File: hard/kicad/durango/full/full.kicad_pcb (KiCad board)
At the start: 2 copper layers, 98 parts, among them J1 NANOLINK, J105 SCART, J2 AUDIO IN, J206 VIDEO, J3 IOX9, J4 BUZZER, J7 POWER, J8 DEBUG, Q1 BC547, Q106 BC547, Q2 BC547, Q3 BC547, Q4 BC547, Q5 BC547, SW1 RESET, SW2 NMI, U1 65C02, U10 74HC139, U104 74HC257, U105 74HC257, U11 74HC688, U12 74HC74, U124 74HC574, U125 74HC257, U126 HC86, U127 74HC245, U13 74HC32, U14 74HC4040, U15 74HCT4040, U16 74HC02, U17 74HC21, U18 74HC85, U19 74HC4040, U2 27C256, U20 74HC85, U204 74HC257, U205 74HC257, U22 74HC175, U224 74HC166, U227 74HC20, U23 74HC86, U3 62256, U31 74HC245, U32 74HC365, U321 74HC257, U528 74HC174, U529 74HC139, U530 74HC367, U6 74HC257, U7 74HC257, U8 74HC132, U9 74HC00, X1 24.576 MHz

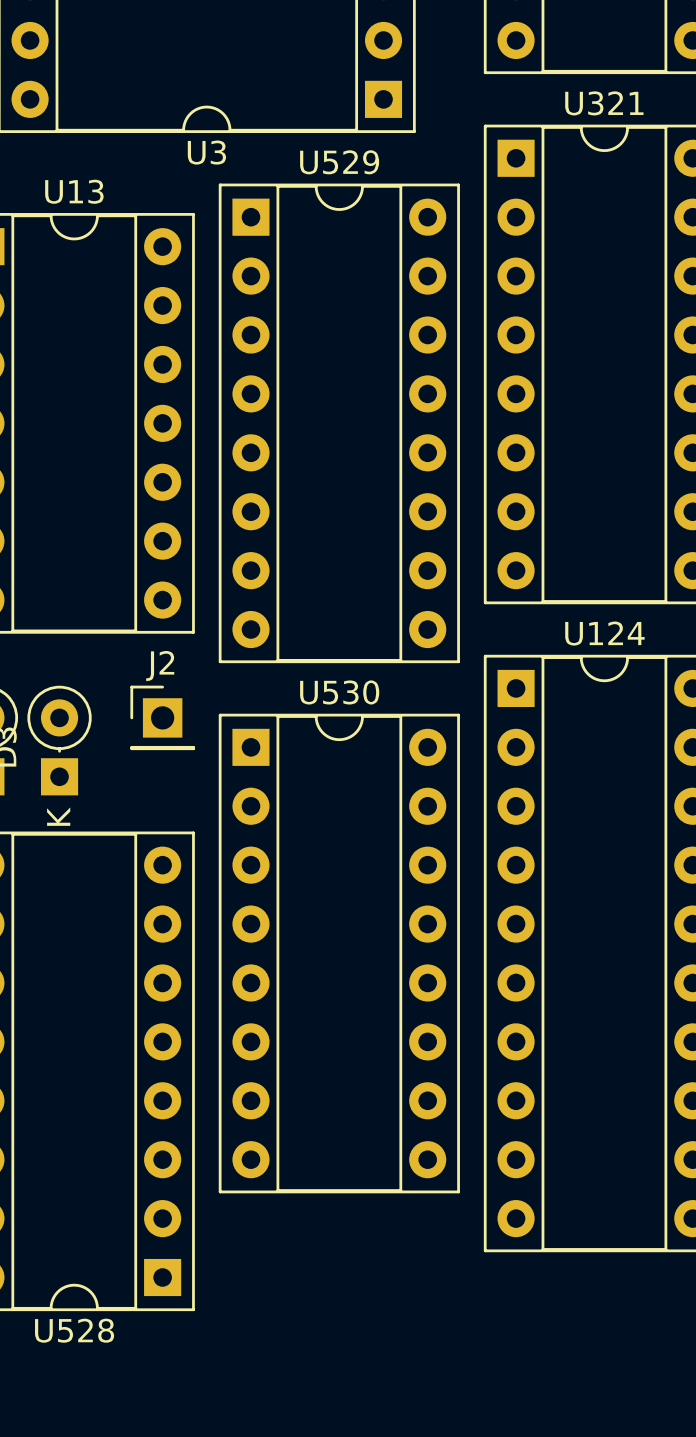
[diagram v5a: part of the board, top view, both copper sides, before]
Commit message: faster extra IO
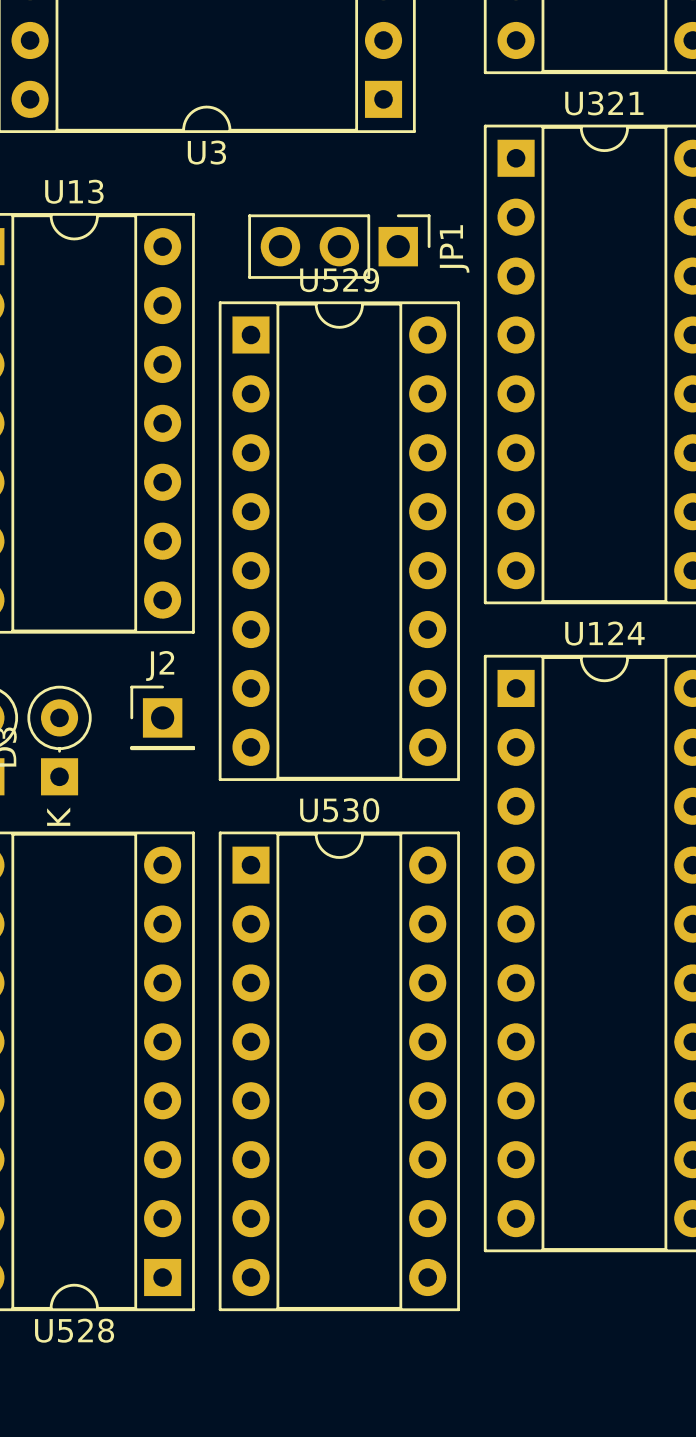
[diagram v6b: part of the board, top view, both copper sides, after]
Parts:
- added JP1: FAST/TIGHT, Connector_PinHeader_2.54mm:PinHeader_1x03_P2.54mm_Vertical, F.Cu at (163.8, 97.8)
- moved U529 5.08 mm to (157.5, 101.6)
- moved U530 5.08 mm to (157.5, 124.5)
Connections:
- U10 pad 13: SCLK -> VCLK
- U529 pad 1: /VDU-X/~IA08 -> /VDU-X/~VFEN
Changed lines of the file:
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@@
     (tracks 215)
     (zones 0)
-    (modules 98)
-    (nets 183)
+    (modules 99)
+    (nets 184)
   )
   (page A4)
@@
   (net 181 /VDU-X/DHRDE)
   (net 182 /VDU-X/HVID)
+  (net 183 /VDU-X/~VFEN)
   (net_class Default "Esta es la clase de red por defecto."
     (clearance 0.2)
@@
     (add_net /VDU-X/~PE)
     (add_net /VDU-X/~VA0)
+    (add_net /VDU-X/~VFEN)
     (add_net /~DWE)
     (add_net /~HIRES)
@@
     (add_net "Net-(D4-Pad2)")
     (add_net "Net-(D6-Pad2)")
+    (add_net "Net-(J105-Pad1)")
+    (add_net "Net-(J105-Pad10)")
+    (add_net "Net-(J105-Pad12)")
+    (add_net "Net-(J105-Pad14)")
+    (add_net "Net-(J105-Pad17)")
+    (add_net "Net-(J105-Pad19)")
+    (add_net "Net-(J105-Pad3)")
     (add_net "Net-(J4-Pad2)")
+    (add_net "Net-(J7-Pad2)")
+    (add_net "Net-(J7-Pad3)")
+    (add_net "Net-(J8-Pad3)")
     (add_net "Net-(Q1-Pad2)")
     (add_net "Net-(Q106-Pad3)")
     (add_net "Net-(Q2-Pad2)")
     (add_net "Net-(Q4-Pad3)")
+    (add_net "Net-(U1-Pad3)")
+    (add_net "Net-(U1-Pad35)")
+    (add_net "Net-(U1-Pad36)")
+    (add_net "Net-(U1-Pad5)")
+    (add_net "Net-(U1-Pad7)")
+    (add_net "Net-(U10-Pad10)")
+    (add_net "Net-(U10-Pad11)")
+    (add_net "Net-(U10-Pad12)")
+    (add_net "Net-(U12-Pad6)")
     (add_net "Net-(U124-Pad12)")
     (add_net "Net-(U124-Pad13)")
@@
     (add_net "Net-(U126-Pad8)")
     (add_net "Net-(U14-Pad1)")
+    (add_net "Net-(U14-Pad12)")
+    (add_net "Net-(U14-Pad13)")
+    (add_net "Net-(U14-Pad14)")
     (add_net "Net-(U14-Pad15)")
+    (add_net "Net-(U14-Pad2)")
+    (add_net "Net-(U14-Pad3)")
+    (add_net "Net-(U14-Pad4)")
+    (add_net "Net-(U14-Pad5)")
+    (add_net "Net-(U14-Pad6)")
+    (add_net "Net-(U14-Pad7)")
+    (add_net "Net-(U14-Pad9)")
+    (add_net "Net-(U15-Pad1)")
     (add_net "Net-(U15-Pad10)")
+    (add_net "Net-(U15-Pad9)")
+    (add_net "Net-(U18-Pad5)")
+    (add_net "Net-(U18-Pad7)")
+    (add_net "Net-(U19-Pad1)")
+    (add_net "Net-(U19-Pad14)")
+    (add_net "Net-(U19-Pad15)")
+    (add_net "Net-(U20-Pad5)")
+    (add_net "Net-(U20-Pad7)")
+    (add_net "Net-(U22-Pad10)")
     (add_net "Net-(U22-Pad11)")
     (add_net "Net-(U22-Pad14)")
+    (add_net "Net-(U22-Pad15)")
+    (add_net "Net-(U22-Pad3)")
+    (add_net "Net-(U22-Pad7)")
     (add_net "Net-(U23-Pad3)")
+    (add_net "Net-(U32-Pad13)")
+    (add_net "Net-(U528-Pad2)")
+    (add_net "Net-(U529-Pad10)")
+    (add_net "Net-(U529-Pad11)")
+    (add_net "Net-(U529-Pad6)")
+    (add_net "Net-(U529-Pad9)")
     (add_net "Net-(U8-Pad3)")
+    (add_net "Net-(X1-Pad1)")
     (add_net R~W)
     (add_net SC0)
@@
     (add_net ~STAT)
   )
+  (module Connector_PinHeader_2.54mm:PinHeader_1x03_P2.54mm_Vertical (layer F.Cu)
+    (at 163.83 97.79 270)
+    (descr "Through hole straight pin header, 1x03, 2.54mm pitch, single row")
+    (tags "Through hole pin header THT 1x03 2.54mm single row")
+    (fp_text reference JP1 (at 0 -2.33 90) (layer F.SilkS)
+      (effects (font (size 1 1) (thickness 0.15)))
+    )
+    (fp_text value FAST/TIGHT (at 0 7.41 90) (layer F.Fab)
+      (effects (font (size 1 1) (thickness 0.15)))
+    )
+    (fp_text user %R (at 0 2.54) (layer F.Fab)
+      (effects (font (size 1 1) (thickness 0.15)))
+    )
+    (fp_line (start 1.8 -1.8) (end -1.8 -1.8) (layer F.CrtYd) (width 0.05))
+    (fp_line (start 1.8 6.85) (end 1.8 -1.8) (layer F.CrtYd) (width 0.05))
+    (fp_line (start -1.8 6.85) (end 1.8 6.85) (layer F.CrtYd) (width 0.05))
+    (fp_line (start -1.8 -1.8) (end -1.8 6.85) (layer F.CrtYd) (width 0.05))
+    (fp_line (start -1.33 -1.33) (end 0 -1.33) (layer F.SilkS) (width 0.12))
+    (fp_line (start -1.33 0) (end -1.33 -1.33) (layer F.SilkS) (width 0.12))
+    (fp_line (start -1.33 1.27) (end 1.33 1.27) (layer F.SilkS) (width 0.12))
+    (fp_line (start 1.33 1.27) (end 1.33 6.41) (layer F.SilkS) (width 0.12))
+    (fp_line (start -1.33 1.27) (end -1.33 6.41) (layer F.SilkS) (width 0.12))
+    (fp_line (start -1.33 6.41) (end 1.33 6.41) (layer F.SilkS) (width 0.12))
+    (fp_line (start -1.27 -0.635) (end -0.635 -1.27) (layer F.Fab) (width 0.1))
+    (fp_line (start -1.27 6.35) (end -1.27 -0.635) (layer F.Fab) (width 0.1))
+    (fp_line (start 1.27 6.35) (end -1.27 6.35) (layer F.Fab) (width 0.1))
+    (fp_line (start 1.27 -1.27) (end 1.27 6.35) (layer F.Fab) (width 0.1))
+    (fp_line (start -0.635 -1.27) (end 1.27 -1.27) (layer F.Fab) (width 0.1))
+    (pad 3 thru_hole oval (at 0 5.08 270) (size 1.7 1.7) (drill 1) (layers *.Cu *.Mask)
+      (net 166 /VDU-X/~IA08))
+    (pad 2 thru_hole oval (at 0 2.54 270) (size 1.7 1.7) (drill 1) (layers *.Cu *.Mask)
+      (net 183 /VDU-X/~VFEN))
+    (pad 1 thru_hole rect (at 0 0 270) (size 1.7 1.7) (drill 1) (layers *.Cu *.Mask)
+      (net 34 ~IO8Q))
+    (model ${KISYS3DMOD}/Connector_PinHeader_2.54mm.3dshapes/PinHeader_1x03_P2.54mm_Vertical.wrl
+      (at (xyz 0 0 0))
+      (scale (xyz 1 1 1))
+      (rotate (xyz 0 0 0))
+    )
+  )
   (module Resistor_THT:R_Axial_DIN0204_L3.6mm_D1.6mm_P2.54mm_Vertical (layer F.Cu)
     (at 191.77 92.075)
@@
   )
   (module Package_DIP:DIP-16_W7.62mm_Socket (layer F.Cu)
-    (at 157.48 119.38)
+    (at 157.48 124.46)
     (descr "16-lead though-hole mounted DIP package, row spacing 7.62 mm (300 mils), Socket")
     (tags "THT DIP DIL PDIP 2.54mm 7.62mm 300mil Socket")
@@
   )
   (module Package_DIP:DIP-16_W7.62mm_Socket (layer F.Cu)
-    (at 157.48 96.52)
+    (at 157.48 101.6)
     (descr "16-lead though-hole mounted DIP package, row spacing 7.62 mm (300 mils), Socket")
     (tags "THT DIP DIL PDIP 2.54mm 7.62mm 300mil Socket")
@@
     (pad 9 thru_hole oval (at 7.62 17.78) (size 1.6 1.6) (drill 0.8) (layers *.Cu *.Mask))
     (pad 1 thru_hole rect (at 0 0) (size 1.6 1.6) (drill 0.8) (layers *.Cu *.Mask)
-      (net 166 /VDU-X/~IA08))
+      (net 183 /VDU-X/~VFEN))
     (model ${KISYS3DMOD}/Package_DIP.3dshapes/DIP-16_W7.62mm_Socket.wrl
       (at (xyz 0 0 0))
@@
       (net 52 /~IOAQ))
     (pad 13 thru_hole oval (at 7.62 7.62) (size 1.6 1.6) (drill 0.8) (layers *.Cu *.Mask)
-      (net 41 SCLK))
+      (net 120 VCLK))
     (pad 5 thru_hole oval (at 0 10.16) (size 1.6 1.6) (drill 0.8) (layers *.Cu *.Mask)
       (net 40 /~IO9Q))

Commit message: PCB updates
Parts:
- added J4: BUZZER, Connector_PinHeader_2.54mm:PinHeader_1x04_P2.54mm_Vertical, F.Cu at (223.5, 78.7)
- added R23: 22, Resistor_THT:R_Axial_DIN0204_L3.6mm_D1.6mm_P2.54mm_Vertical, F.Cu at (224.8, 94.0)
- C1: value 1uF -> 10uF
- C2: value 470nF -> 100nF
- C3: value 47uF -> 10uF
- C4: value 10uF -> 100uF
- C5: value 470uF -> 100uF
- D4: value INT. DISABLED -> ERROR
- R3: value 22K -> 3K3
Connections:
- C4 pad 1: /VDU-X/BIAS -> +5V
- J105 pad 1: (no net) -> Net-(J105-Pad1)
- J105 pad 10: (no net) -> Net-(J105-Pad10)
- J105 pad 12: (no net) -> Net-(J105-Pad12)
- J105 pad 14: (no net) -> Net-(J105-Pad14)
- J105 pad 17: (no net) -> Net-(J105-Pad17)
- J105 pad 19: (no net) -> Net-(J105-Pad19)
- J105 pad 3: (no net) -> Net-(J105-Pad3)
- J7 pad 2: (no net) -> Net-(J7-Pad2)
- J7 pad 3: (no net) -> Net-(J7-Pad3)
- J8 pad 3: (no net) -> Net-(J8-Pad3)
- Q3 pad 3: Net-(J4-Pad2) -> Net-(Q3-Pad3)
- R4 pad 2: Net-(J4-Pad2) -> Net-(Q3-Pad3)
- U1 pad 3: (no net) -> Net-(U1-Pad3)
- U1 pad 35: (no net) -> Net-(U1-Pad35)
- U1 pad 36: (no net) -> Net-(U1-Pad36)
- U1 pad 5: (no net) -> Net-(U1-Pad5)
- U1 pad 7: (no net) -> Net-(U1-Pad7)
- U10 pad 10: (no net) -> Net-(U10-Pad10)
- U10 pad 11: (no net) -> Net-(U10-Pad11)
- U10 pad 12: (no net) -> Net-(U10-Pad12)
- U12 pad 6: (no net) -> Net-(U12-Pad6)
- U14 pad 12: (no net) -> Net-(U14-Pad12)
- U14 pad 13: (no net) -> Net-(U14-Pad13)
- U14 pad 14: (no net) -> Net-(U14-Pad14)
- U14 pad 2: (no net) -> Net-(U14-Pad2)
- U14 pad 3: (no net) -> Net-(U14-Pad3)
- U14 pad 4: (no net) -> Net-(U14-Pad4)
- U14 pad 5: (no net) -> Net-(U14-Pad5)
- U14 pad 6: (no net) -> Net-(U14-Pad6)
- U14 pad 7: (no net) -> Net-(U14-Pad7)
- U14 pad 9: (no net) -> Net-(U14-Pad9)
- U15 pad 1: (no net) -> Net-(U15-Pad1)
- U15 pad 9: (no net) -> Net-(U15-Pad9)
- U18 pad 5: (no net) -> Net-(U18-Pad5)
- U18 pad 7: (no net) -> Net-(U18-Pad7)
- U19 pad 1: (no net) -> Net-(U19-Pad1)
- U19 pad 14: (no net) -> Net-(U19-Pad14)
- U19 pad 15: (no net) -> Net-(U19-Pad15)
- U20 pad 5: (no net) -> Net-(U20-Pad5)
- U20 pad 7: (no net) -> Net-(U20-Pad7)
- U22 pad 10: (no net) -> Net-(U22-Pad10)
- U22 pad 15: (no net) -> Net-(U22-Pad15)
- U22 pad 3: (no net) -> Net-(U22-Pad3)
- U22 pad 7: (no net) -> Net-(U22-Pad7)
- U32 pad 13: (no net) -> Net-(U32-Pad13)
- U528 pad 2: (no net) -> Net-(U528-Pad2)
- U529 pad 10: (no net) -> Net-(U529-Pad10)
- U529 pad 11: (no net) -> Net-(U529-Pad11)
- U529 pad 6: (no net) -> Net-(U529-Pad6)
- U529 pad 9: (no net) -> Net-(U529-Pad9)
- X1 pad 1: (no net) -> Net-(X1-Pad1)

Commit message: new component footprints
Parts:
- removed the J4 at (134.6, 130.8)
- C1, C3, C4: footprint Capacitor_THT:CP_Radial_D5.0mm_P2.50mm -> Capacitor_THT:CP_Radial_D4.0mm_P1.50mm
- C2, C7: footprint Capacitor_THT:C_Disc_D4.7mm_W2.5mm_P5.00mm -> Capacitor_THT:C_Rect_L7.2mm_W2.5mm_P5.00mm_FKS2_FKP2_MKS2_MKP2
- C5: footprint Capacitor_THT:CP_Radial_D10.0mm_P5.00mm -> Capacitor_THT:CP_Radial_D4.0mm_P1.50mm
- C6: footprint Capacitor_THT:CP_Radial_D10.0mm_P5.00mm -> Capacitor_THT:CP_Radial_D6.3mm_P2.50mm
- C8: footprint Capacitor_THT:C_Disc_D4.7mm_W2.5mm_P5.00mm -> Capacitor_THT:C_Disc_D3.0mm_W2.0mm_P2.50mm
- R1, R107, R108, R109, R110, R111, R112, R113, R114, R127, R128, R15, R16, R17, R18, R19, R2, R21, R220, R229, R23, R26, R29, R3, R4, R5, R6, R824, R825: footprint Resistor_THT:R_Axial_DIN0204_L3.6mm_D1.6mm_P2.54mm_Vertical -> Resistor_THT:R_Axial_DIN0207_L6.3mm_D2.5mm_P2.54mm_Vertical
- R122: footprint Resistor_THT:R_Axial_DIN0204_L3.6mm_D1.6mm_P2.54mm_Vertical -> Resistor_THT:R_Axial_DIN0309_L9.0mm_D3.2mm_P2.54mm_Vertical
- moved J4 85.2 mm to (168.9, 144.1), turned to 90 degrees
- moved R23 62.5 mm to (182.9, 140.3), turned to 180 degrees
- moved D6 10.2 mm to (64.8, 66.0)
- moved R29 10.2 mm to (64.8, 71.1)
- moved RN1 10.2 mm to (71.1, 71.1)
- moved J1 9.52 mm to (64.8, 51.4)
- moved Q2 5.71 mm to (69.8, 83.8)
- moved SW2 5.68 mm to (71.1, 78.7)
- moved Q1 4.44 mm to (70.5, 92.7)
- moved R1 4.44 mm to (66.0, 91.4)
- moved R2 4.44 mm to (66.0, 83.8)
- moved D1 3.18 mm to (71.1, 95.9)
- moved SW1 3.17 mm to (64.8, 99.7)
- moved R4 2.54 mm to (182.9, 144.1)
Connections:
- J105 pad 1: Net-(J105-Pad1) -> (no net)
- J105 pad 10: Net-(J105-Pad10) -> (no net)
- J105 pad 12: Net-(J105-Pad12) -> (no net)
- J105 pad 14: Net-(J105-Pad14) -> (no net)
- J105 pad 17: Net-(J105-Pad17) -> (no net)
- J105 pad 19: Net-(J105-Pad19) -> (no net)
- J105 pad 3: Net-(J105-Pad3) -> (no net)
- J4 pad 2: Net-(J4-Pad2) -> (no net)
- J4 pad 3: Net-(J4-Pad3) -> (no net)
- J7 pad 2: Net-(J7-Pad2) -> (no net)
- J7 pad 3: Net-(J7-Pad3) -> (no net)
- J8 pad 3: Net-(J8-Pad3) -> (no net)
- U1 pad 3: Net-(U1-Pad3) -> (no net)
- U1 pad 35: Net-(U1-Pad35) -> (no net)
- U1 pad 36: Net-(U1-Pad36) -> (no net)
- U1 pad 5: Net-(U1-Pad5) -> (no net)
- U1 pad 7: Net-(U1-Pad7) -> (no net)
- U10 pad 10: Net-(U10-Pad10) -> (no net)
- U10 pad 11: Net-(U10-Pad11) -> (no net)
- U10 pad 12: Net-(U10-Pad12) -> (no net)
- U12 pad 6: Net-(U12-Pad6) -> (no net)
- U14 pad 12: Net-(U14-Pad12) -> (no net)
- U14 pad 13: Net-(U14-Pad13) -> (no net)
- U14 pad 14: Net-(U14-Pad14) -> (no net)
- U14 pad 2: Net-(U14-Pad2) -> (no net)
- U14 pad 3: Net-(U14-Pad3) -> (no net)
- U14 pad 4: Net-(U14-Pad4) -> (no net)
- U14 pad 5: Net-(U14-Pad5) -> (no net)
- U14 pad 6: Net-(U14-Pad6) -> (no net)
- U14 pad 7: Net-(U14-Pad7) -> (no net)
- U14 pad 9: Net-(U14-Pad9) -> (no net)
- U15 pad 1: Net-(U15-Pad1) -> (no net)
- U15 pad 9: Net-(U15-Pad9) -> (no net)
- U18 pad 5: Net-(U18-Pad5) -> (no net)
- U18 pad 7: Net-(U18-Pad7) -> (no net)
- U19 pad 1: Net-(U19-Pad1) -> (no net)
- U19 pad 14: Net-(U19-Pad14) -> (no net)
- U19 pad 15: Net-(U19-Pad15) -> (no net)
- U20 pad 5: Net-(U20-Pad5) -> (no net)
- U20 pad 7: Net-(U20-Pad7) -> (no net)
- U22 pad 10: Net-(U22-Pad10) -> (no net)
- U22 pad 15: Net-(U22-Pad15) -> (no net)
- U22 pad 3: Net-(U22-Pad3) -> (no net)
- U22 pad 7: Net-(U22-Pad7) -> (no net)
- U32 pad 13: Net-(U32-Pad13) -> (no net)
- U528 pad 2: Net-(U528-Pad2) -> (no net)
- U529 pad 10: Net-(U529-Pad10) -> (no net)
- U529 pad 11: Net-(U529-Pad11) -> (no net)
- U529 pad 6: Net-(U529-Pad6) -> (no net)
- U529 pad 9: Net-(U529-Pad9) -> (no net)
- X1 pad 1: Net-(X1-Pad1) -> (no net)
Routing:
- net /~SO: track 20.1 -> 29.5 mm
- net /RDY: track 3.81 -> 12.5 mm
- net /~IRQ: track 3.81 -> 12.5 mm
- net /~NMI: track 4.86 -> 9.94 mm
- net +5V: track 3.81 -> 7.40 mm
- net Net-(D6-Pad2): track 2.54 -> 0.00 mm
